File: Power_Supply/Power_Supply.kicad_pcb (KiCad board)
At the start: 2 copper layers, 100 x 50 mm, 65 parts, among them J1 ICSP, J2 Conn_01x01, J3 Conn_01x01, J4 Screw_Terminal_01x02, SW1 UP, SW2 DW, SW3 V_I_SEL, SW4 O_EN, U1 L78L08_SOT89, U2 ATmega328PB-AU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

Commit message: did via stitching for ground
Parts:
- added J6: Conn_01x04, Custom_Vertical_1x_2.54mm_Pin_Header:PinHeader_1x04_P2.54mm_Vertical, F.Cu at (22.0, 15.0)
- added J7: Conn_01x04, Custom_Vertical_1x_2.54mm_Pin_Header:PinHeader_1x04_P2.54mm_Vertical, F.Cu at (56.0, 15.0)
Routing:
- net /SCL0: track 0.00 -> 106.5 mm, vias 0 -> 2
- net /SDA0: track 0.00 -> 104.5 mm
- net +5V: track 171.6 -> 213.8 mm
- net GND: track 12.7 -> 25.7 mm, vias 4 -> 83
- net /V_SENSE: track 40.3 -> 37.4 mm
- net Net-(D2-Pad1): track 11.9 -> 10.0 mm, vias 3 -> 2

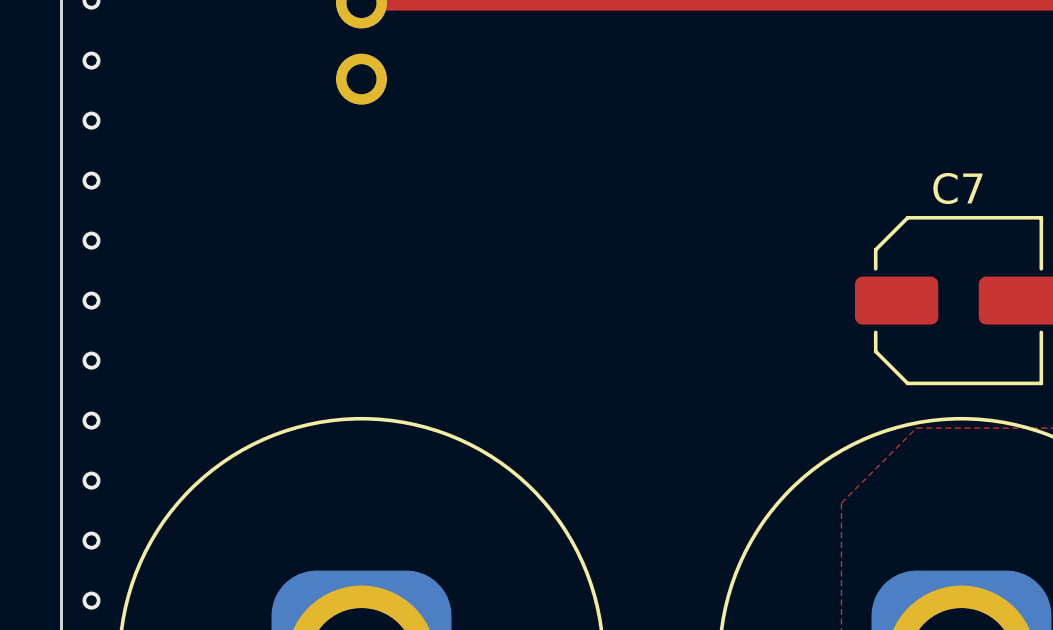
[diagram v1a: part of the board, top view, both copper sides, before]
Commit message: layout complete - need to clean scehmatic, add logo, generate gerber/BOM
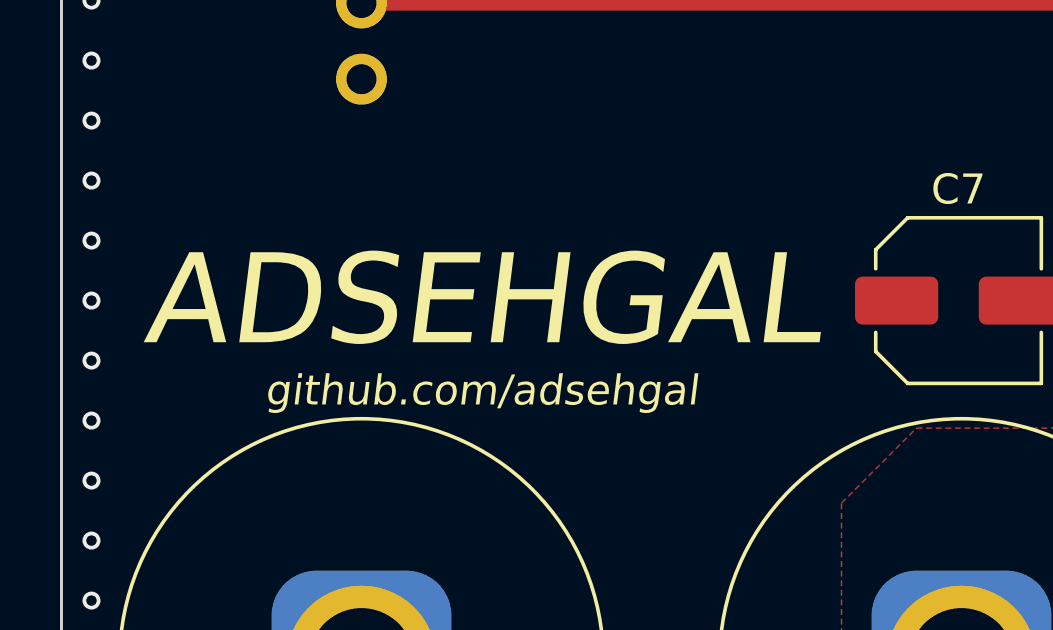
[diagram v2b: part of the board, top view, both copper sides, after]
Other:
- board text added: "ADSEHGAL"
- board text added: "github.com/adsehgal"
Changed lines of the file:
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@@
   (general
     (thickness 1.6)
-    (drawings 19)
-    (tracks 609)
+    (drawings 21)
+    (tracks 526)
     (modules 67)
     (nets 50)
@@
   (gr_line (start 59 25) (end 59 12) (layer "F.CrtYd") (width 0.05))
   (gr_line (start 19 12) (end 19 25) (layer "F.CrtYd") (width 0.05))
+  (gr_text "github.com/adsehgal" (at 26 33) (layer "F.SilkS")
+    (effects (font (size 1 1) (thickness 0.075) italic))
+  )
+  (gr_text "ADSEHGAL" (at 26 30) (layer "F.SilkS")
+    (effects (font (size 3 3) (thickness 0.75) italic))
+  )
   (dimension 13 (width 0.15) (layer "Dwgs.User")
     (gr_text "13.000 mm" (at -0.3 18.5 270) (layer "Dwgs.User")
